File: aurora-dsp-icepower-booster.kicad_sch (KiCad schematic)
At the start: 230 parts, among them J1 XLR_IN_1, J10 XLR3_OUT, J11 XLR3_OUT, J12 XLR3_OUT, J13 24V DC, J2 XLR_IN_2, J3 XLR_IN_3, J4 XLR_IN_4, J5 XLR_IN_5, J6 XLR_IN_6, J7 XLR3_OUT, J8 XLR3_OUT, J9 XLR3_OUT, SW1 Gain CH1, SW2 Gain CH2, SW3 Gain CH3, SW4 Gain CH4, SW5 Gain CH5, SW6 Gain CH6, U1 LM4562, U10 LM4562, U11 LM4562, U12 LM4562, U13 TEL5-2422, U14 ADP7118ARDZ-11, U15 ADP7182AUJZ-11, U2 LM4562, U3 LM4562, U4 LM4562, U5 LM4562, U6 LM4562, U7 LM4562, U8 LM4562, U9 LM4562

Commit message: chore: 🔄 update code structure for better maintainability
* Refactored multiple code sections to improve readability.
* Removed redundant code blocks to streamline functionality.
* Enhanced modularity for easier future updates.
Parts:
- added C77, C78: 100nF C0G, Capacitor_SMD:C_0805_2012Metric, symbol Device:C
- C11, C12, C15, C16, C19, C20, C23, C24, C3, C4, C7, C8: value 100n -> 100nF C0G
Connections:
- net +12V: now also C77.2
- net -12V: now also C78.1
- net GND: now also C77.1, C78.2

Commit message: chore: 🔄 empty code changes
* No code changes were made in this commit.
* This serves as a placeholder for future updates.
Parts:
- added C79, C81, C82: 100nF C0G, Capacitor_SMD:C_0805_2012Metric, symbol Device:C
- added D25: SMBJ15CA, Diode_SMD:D_SMB, symbol Device:D_TVS
- added J14: REMOTE 3.5mm, Connector_Audio:AudioJack2_Ground_Switch_Lumberg_1503_09, symbol Connector:Barrel_Jack
- added R105: 10k, Resistor_SMD:R_0805_2012Metric, symbol Device:R
- added SW7: ALWAYS/REMOTE, Connector_PinHeader_2.54mm:PinHeader_1x03_P2.54mm_Vertical, symbol Switch:SW_SPDT
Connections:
- net +12V: now also U13.24 (+VOUT), U14.6 (VIN), SW7.1 (A); no longer J13.2, R79.1, R80.1, U13.14 (-VOUT), U13.7 (-VIN), U14.4 (EN)
- net -12V: now also U13.14 (-VOUT), U15.2 (VIN); no longer U13.24 (+VOUT), U15.3 (EN)
- net GND: now also C51.2, C52.2, J13.2, R79.2, R80.2, U13.7 (-VIN), U14.3 (GND), U14.7 (GND), U15.1 (GND), C79.2, C81.2, C82.2, D25.2 (A2), J14.2
- net V+: now also U14.1 (VOUT), U14.2 (SENSE/ADJ); no longer U14.5 (SS)
- net V-: now also U15.5 (VOUT)
- net +24V_IN: now reaches J13.1, U13.1 (+VIN)
- net NR_U15: now reaches U15.4 (ADJ)
- net NR_U15: now also C82.1
- new net EN_CTRL: R79.1, R80.1, SW7.2 (B), U14.4 (EN), U15.3 (EN)
- new net REMOTE_FILT: C79.1, R105.2, SW7.3 (C)
- new net REMOTE_IN: D25.1 (A1), J14.1, R105.1
- new net SS_U14: C81.1, U14.5 (SS)

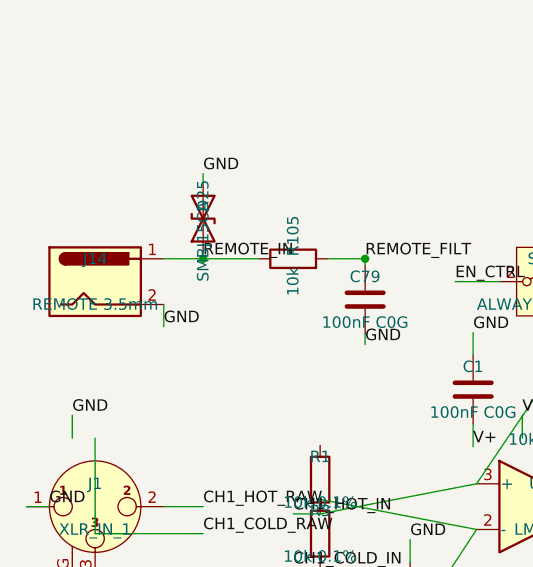
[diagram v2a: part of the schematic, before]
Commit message: feat(aurora-dsp-icepower-booster): 🎛️ update audio jack component and metadata
* Changed the footprint of `J14` from `Connector_Audio:AudioJack2_Ground_Switch_Lumberg_1503_09` to `Connector_Audio:Jack_3.5mm_Lumberg_1503_02_Horizontal`.
* Updated the `libsource` and `fields` for `J14` to reflect the new audio jack specifications.
* Adjusted the pin references for `J14` in the net connections to match the new footprint.
* Added a new library part for `AudioJack2` with relevant fields and pins.
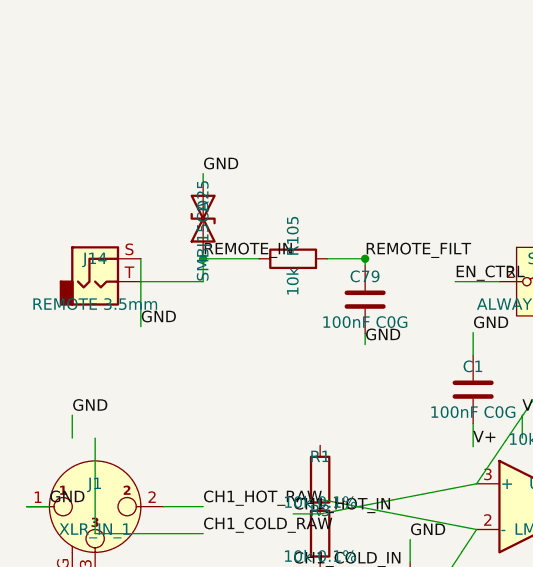
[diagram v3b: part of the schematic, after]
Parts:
- J14: footprint Connector_Audio:AudioJack2_Ground_Switch_Lumberg_1503_09 -> Connector_Audio:Jack_3.5mm_Lumberg_1503_02_Horizontal; symbol Connector:Barrel_Jack -> Connector_Audio:AudioJack2
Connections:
- net GND: now also J14.S; no longer J14.2
- net REMOTE_IN: now also J14.T; no longer J14.1

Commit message: chore: 🔄 update code structure for better maintainability
* Refactored multiple code sections to improve readability.
* Removed redundant code blocks to streamline functionality.
* Enhanced comments for clarity on complex logic.
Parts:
- added unit 3 of U1
- added unit 3 of U10
- added unit 3 of U11
- added unit 3 of U12
- added unit 3 of U2
- added unit 3 of U3
- added unit 3 of U4
- added unit 3 of U5
- added unit 3 of U6
- added unit 3 of U7
- added unit 3 of U8
- added unit 3 of U9
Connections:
- net CH1_COLD_RAW: now also J1.3
- net CH1_HOT_RAW: now also J7.3
- net CH1_RX_OUT: now also R2.2, U1.1
- net CH2_COLD_RAW: now also J2.3
- net CH2_HOT_RAW: now also J8.3
- net CH2_RX_OUT: now also R15.2, U2.1
- net CH3_COLD_RAW: now also J3.3
- net CH3_HOT_RAW: now also J9.3
- net CH3_RX_OUT: now also R28.2, U3.1
- net CH4_COLD_RAW: now also J4.3
- net CH4_HOT_RAW: now also J10.3
- net CH4_RX_OUT: now also R41.2, U4.1
- net CH5_COLD_RAW: now also J5.3
- net CH5_HOT_RAW: now also J11.3
- net CH5_RX_OUT: now also R54.2, U5.1
- net CH6_COLD_RAW: now also J6.3
- net CH6_HOT_RAW: now also J12.3
- net CH6_RX_OUT: now also R67.2, U6.1
- net GND: now also J1.G, J2.G, J3.G, J4.G, J5.G, J6.G
- net V+: now also U1.8 (V+), U10.8 (V+), U11.8 (V+), U12.8 (V+), U2.8 (V+), U3.8 (V+), U4.8 (V+), U5.8 (V+), U6.8 (V+), U7.8 (V+), U8.8 (V+), U9.8 (V+)
- net V-: now also U1.4 (V-), U10.4 (V-), U11.4 (V-), U12.4 (V-), U2.4 (V-), U3.4 (V-), U4.4 (V-), U5.4 (V-), U6.4 (V-), U7.4 (V-), U8.4 (V-), U9.4 (V-)
- no-connect marks 0 -> 1
